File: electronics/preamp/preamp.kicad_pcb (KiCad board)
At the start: 2 copper layers, 25 x 25 mm, 27 parts, among them J1 Conn_01x01, J2 Conn_01x01, J3 Conn_01x05, U1 TL064

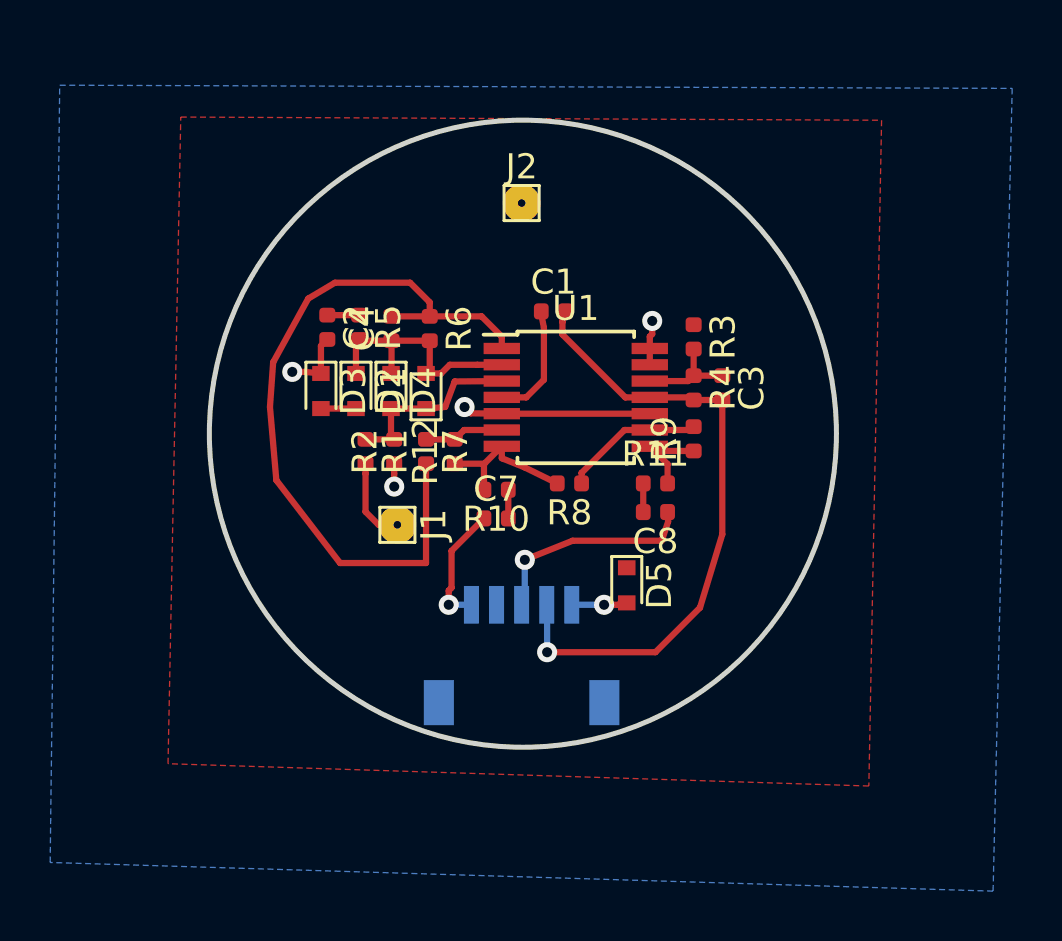
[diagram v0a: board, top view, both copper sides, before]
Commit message: preamp: Tweak layout
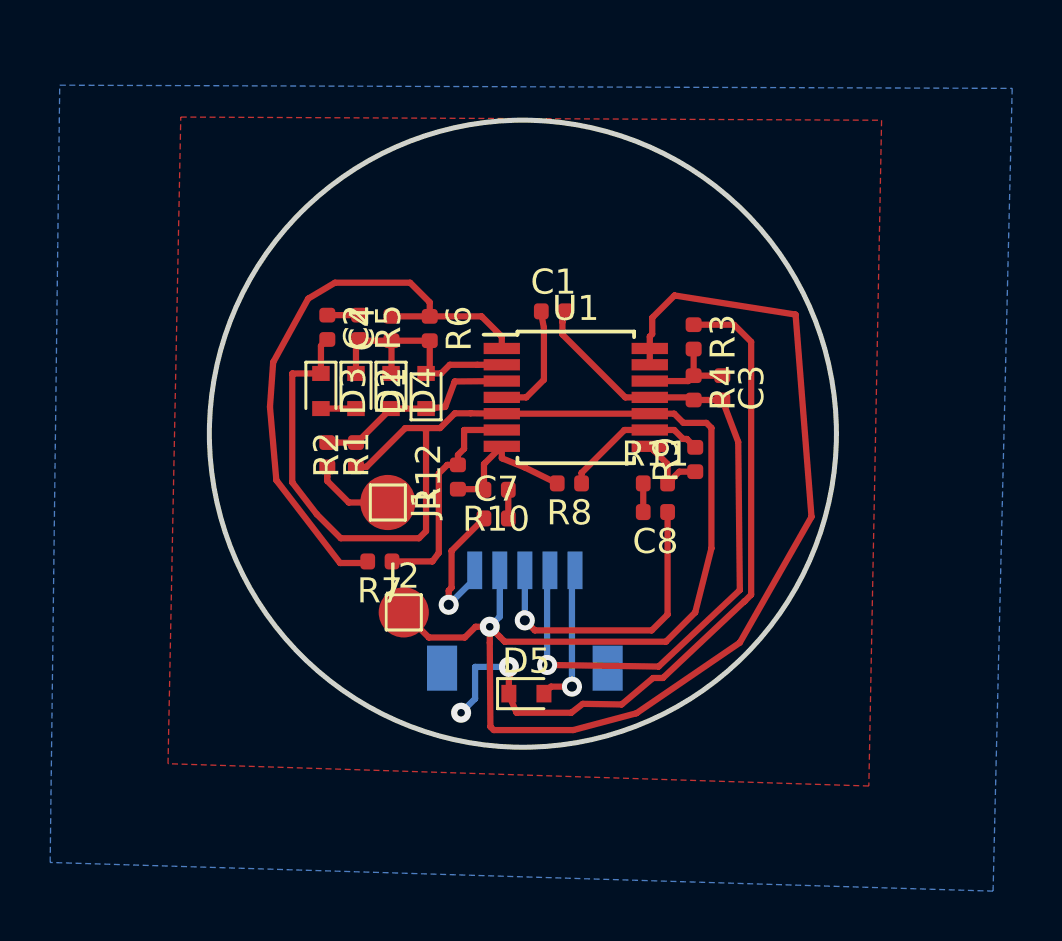
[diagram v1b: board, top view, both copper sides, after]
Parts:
- moved J2 17.0 mm to (95.2, 107.1)
- moved D5 5.89 mm to (100.1, 110.4), turned to 0 degrees
- moved R7 4.75 mm to (94.3, 105.1), turned to 180 degrees
- moved R1 1.53 mm to (92.2, 100.8)
- moved R2 1.53 mm to (93.3, 100.8)
- moved J3 1.38 mm to (100.1, 107.5)
- moved R12 1.02 mm to (97.4, 101.7)
- moved J1 0.97 mm to (94.6, 102.7)
- moved R9 0.83 mm to (106.9, 101.0)
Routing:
- net VGND: track 12.8 -> 92.4 mm, vias 4 -> 1
- net VCC: track 4.81 -> 34.0 mm, vias 0 -> 2
- net /AMP: track 30.5 -> 24.0 mm
- net /GAIN-: track 3.17 -> 9.10 mm
- net +BATT: track 1.88 -> 6.13 mm
- net /OUT-: track 8.64 -> 12.2 mm
- net -BATT: track 25.5 -> 28.8 mm
- net /OUT+: track 4.93 -> 5.83 mm
- net /IN+: track 3.40 -> 4.08 mm
- net /PRE+: track 7.60 -> 8.28 mm

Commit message: preamp: Cleanup layout a bit
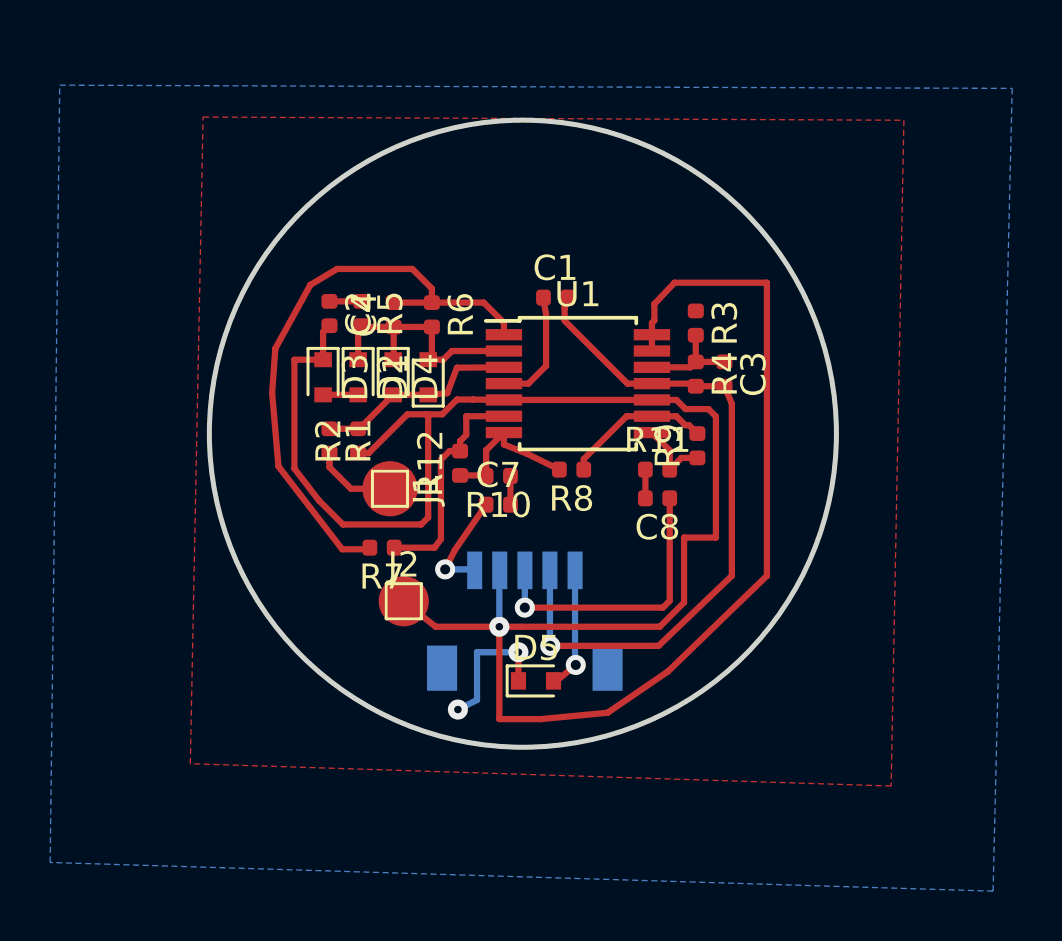
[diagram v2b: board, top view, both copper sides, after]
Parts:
- moved D5 0.64 mm to (100.5, 109.9)
- moved D3 0.56 mm to (92.0, 97.7)
- moved C1 0.56 mm to (101.3, 94.6)
- moved C3 0.56 mm to (108.0, 97.6)
- moved C4 0.56 mm to (94.8, 95.3)
- moved C7 0.56 mm to (99.0, 102.8)
- moved D1 0.56 mm to (96.2, 97.7)
- moved D2 0.56 mm to (93.4, 97.7)
- moved D4 0.56 mm to (94.8, 97.7)
- moved R10 0.56 mm to (99.0, 101.7)
- moved R12 0.56 mm to (97.5, 101.2)
- moved R4 0.56 mm to (106.9, 97.6)
- moved R6 0.56 mm to (96.4, 95.3)
- moved R7 0.56 mm to (94.4, 104.5)
- moved U1 0.56 mm to (102.2, 98.0)
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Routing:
- net VCC: track 34.0 -> 10.4 mm
- net VGND: track 92.4 -> 90.6 mm
- net /OUT+: track 5.83 -> 4.25 mm
- net -BATT: track 28.8 -> 27.6 mm
- net +BATT: track 6.13 -> 5.31 mm
- net /OUT-: track 12.2 -> 11.5 mm
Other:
- board text removed: "OUT"

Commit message: preamp: Add artwork
- Import PNG into bitmap2component
- Adjust tresholds to export mask and silkscreen
- Merge the two files into one kicad_mod
- Import the footprint, flip to back and rotate
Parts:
- added G***: LOGO, piezopro:art, B.Cu at (100.3, 96.9)
- J3: footprint Connector_Molex:Molex_Pico-Clasp_202396-0507_1x05-1MP_P1.00mm_Horizontal -> piezopro:Molex_Pico-Clasp_202396-0507_1x05-1MP_P1.00mm_Horizontal_NoSilk
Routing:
- net VCC: track 10.4 -> 9.00 mm

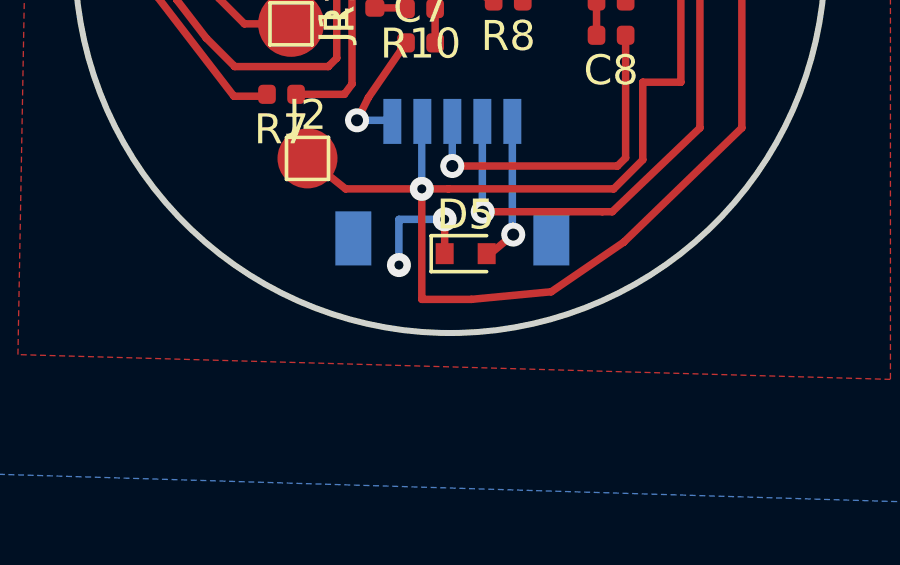
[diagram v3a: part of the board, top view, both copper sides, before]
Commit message: preamp: Add edge plating connector
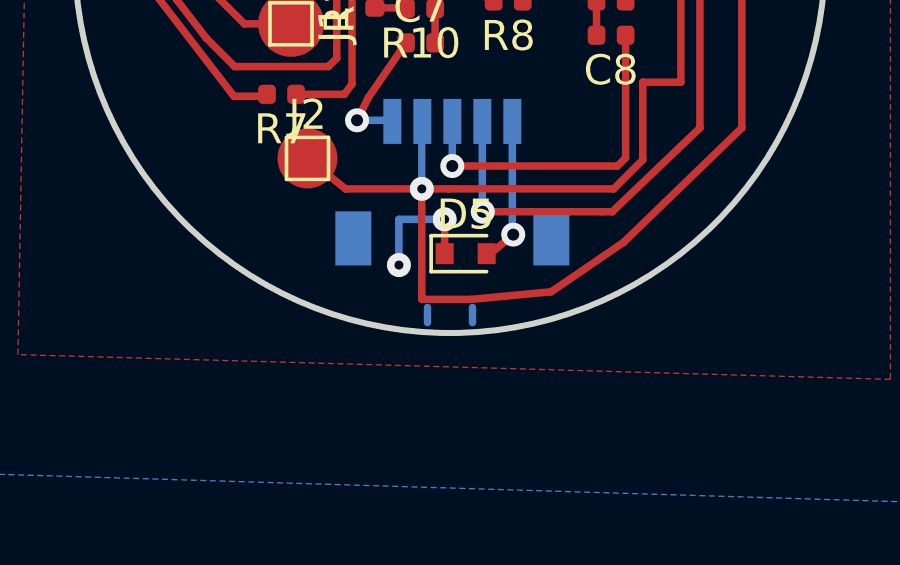
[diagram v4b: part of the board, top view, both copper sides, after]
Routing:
- net (no net): track 0.00 -> 1.00 mm
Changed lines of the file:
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@@
   (general
     (thickness 1.6)
-    (drawings 64)
-    (tracks 166)
+    (drawings 65)
+    (tracks 168)
     (zones 0)
     (modules 28)
@@
   (page A4)
   (layers
-    (0 F.Cu signal)
+    (0 F.Cu signal hide)
     (31 B.Cu signal)
     (32 B.Adhes user hide)
@@
     (40 Dwgs.User user hide)
     (41 Cmts.User user hide)
-    (42 Eco1.User user hide)
+    (42 Eco1.User user)
     (43 Eco2.User user hide)
     (44 Edge.Cuts user)
@@
     (last_trace_width 0.25)
     (trace_clearance 0.2)
-    (zone_clearance 0.2)
+    (zone_clearance -0.2)
     (zone_45_only no)
     (trace_min 0.2)
@@
       (xy -6.532907 5.894542)) (layer B.SilkS) (width 0.01))
   )
+  (gr_line (start 99.5 112.5) (end 100.5 112.5) (layer Eco1.User) (width 0.2))
   (gr_line (start 89.656453 106.982172) (end 88.504073 104.858851) (layer Eco2.User) (width 0.2))
   (gr_line (start 102.685888 108.3949) (end 103.686012 108.3949) (layer Eco2.User) (width 0.2))
@@
   (gr_circle (center 100 100) (end 110 100) (layer Eco1.User) (width 0.2))
   (gr_circle (center 100 100) (end 112.5 100) (layer Edge.Cuts) (width 0.2))
+  (segment (start 100.75 111.65) (end 100.75 112.15) (width 0.25) (layer B.Cu) (net 0))
+  (segment (start 99.25 111.65) (end 99.25 112.15) (width 0.25) (layer B.Cu) (net 0))
   (segment (start 102.078 105.447) (end 102.078 109.25) (width 0.25) (layer B.Cu) (net 1))
   (segment (start 102.16436 104.89836) (end 102.16436 105.11336) (width 0.25) (layer B.Cu) (net 1))
